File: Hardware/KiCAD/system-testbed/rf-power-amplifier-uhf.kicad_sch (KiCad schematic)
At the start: 22 parts, among them U5 GRF5604

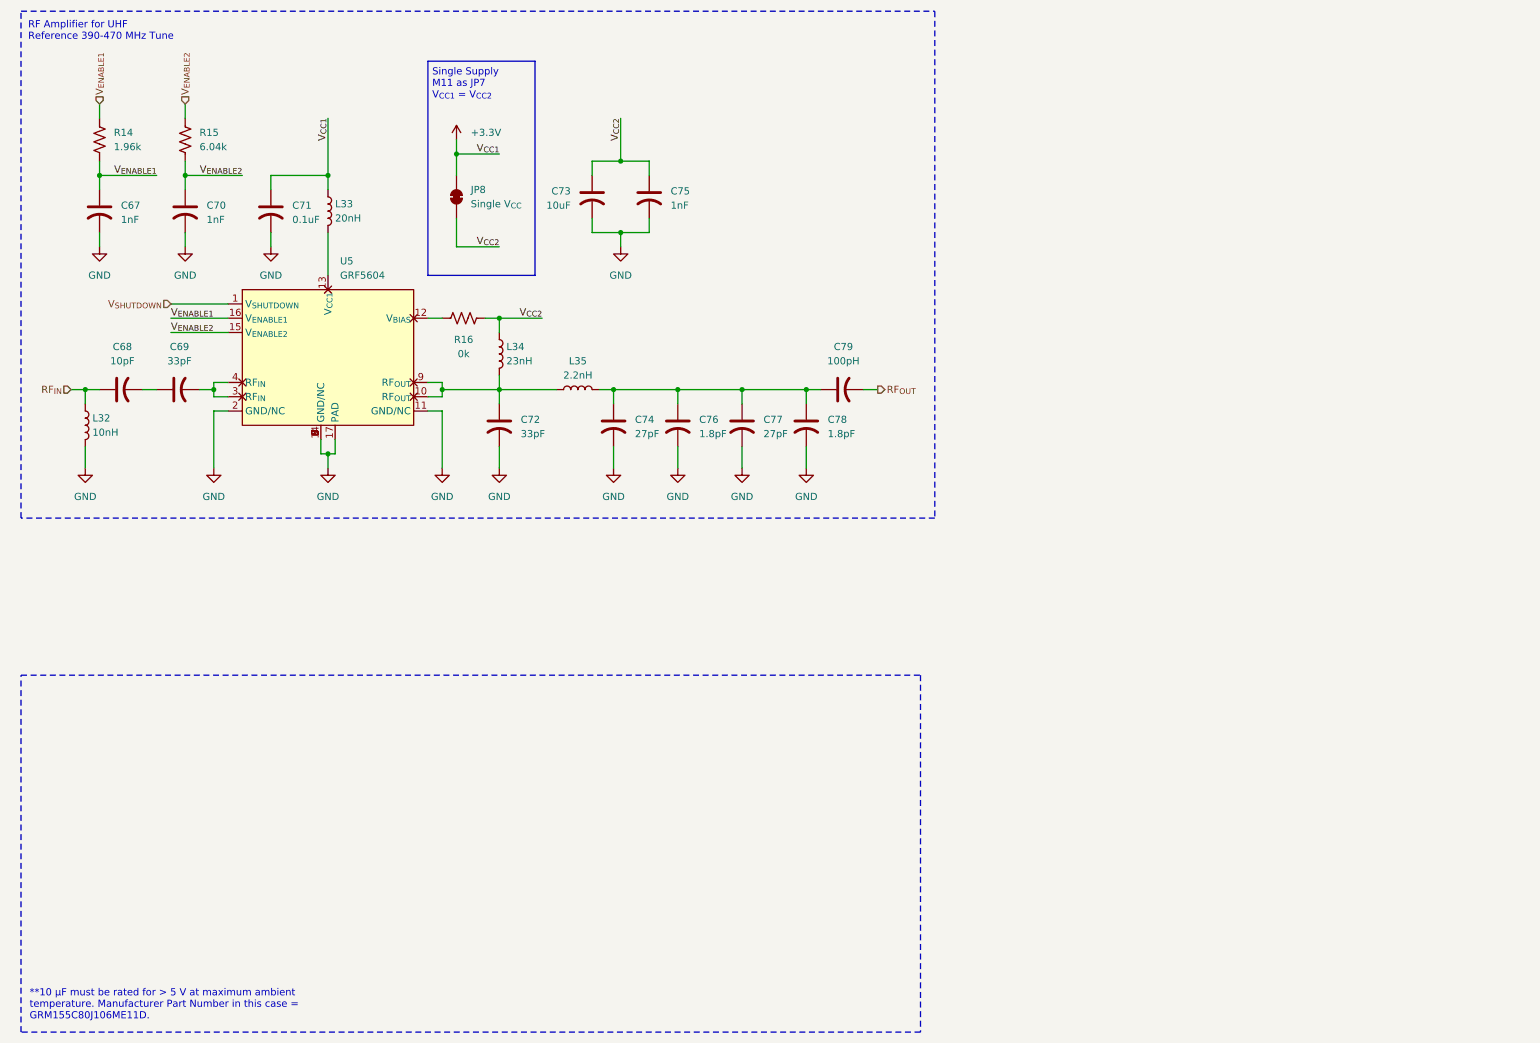
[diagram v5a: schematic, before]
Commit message: feat: separate RF subsystems for testing using SMA edge launches in testbed KiCAD project #65 #34 #45
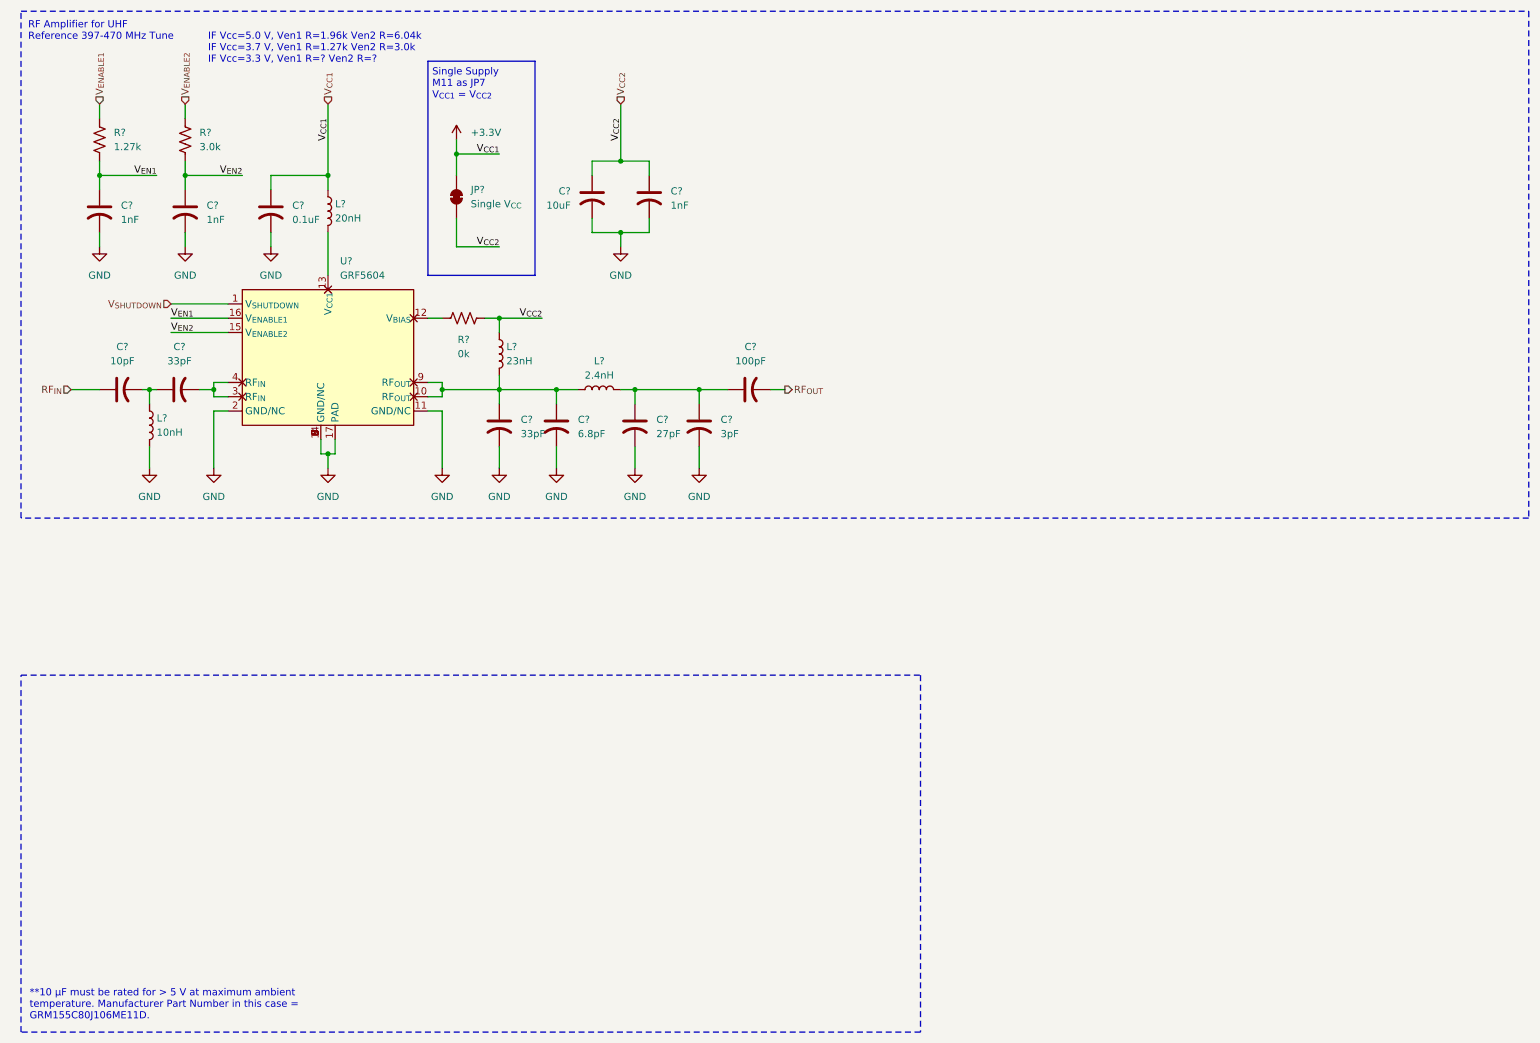
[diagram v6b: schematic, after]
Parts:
- removed C77: 27pF, Capacitor_SMD:C_0402_1005Metric, symbol Device:C_US
- removed C78: 1.8pF, Capacitor_SMD:C_0402_1005Metric, symbol Device:C_US
- added C?: 6.8pF, Capacitor_SMD:C_0402_1005Metric, symbol Device:C_US
- C?: renamed from C79; value 100pH -> 100pF
- C?: renamed from C76; value 1.8pF -> 3pF
- L?: renamed from L35; value 2.2nH -> 2.4nH
- L?: renamed from L34; footprint Inductor_SMD:L_0402_1005Metric -> capstone-project:0908SQ23NGLC
- R?: renamed from R14; value 1.96k -> 1.27k
- R?: renamed from R15; value 6.04k -> 3.0k
- renumbered C74 to C?, C69 to C?, C71 to C?, C75 to C?, C73 to C?, C67 to C?, C72 to C?, C70 to C?, C68 to C?, JP8 to JP?, L32 to L?, L33 to L?, R16 to R?, U5 to U?
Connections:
- net GND: now also C?.2
- net RF_{IN}: no longer L?.1
- net V_{ENABLE1}: no longer C?.1, R?.1, U?.16 (V_{ENABLE1})
- net V_{ENABLE2}: no longer C?.1, R?.1, U?.15 (V_{ENABLE2})
- net at C?.1, L?.1, L?.2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: now also C?.1
- net at C?.1, C?.2: now also L?.1
- new net V_{EN1}: C?.1, R?.1, U?.16 (V_{ENABLE1})
- new net V_{EN2}: C?.1, R?.1, U?.15 (V_{ENABLE2})
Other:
- note added: "IF Vcc=5.0 V, Ven1 R=1.96k Ven2 R=6.04k IF Vcc=3.7 V, Ven1 R=1.27k Ven2 R=3.0k IF Vcc=3.3 V, Ven1 R=? Ven2 R=?"
- note added: "RF Amplifier for UHF Reference 397-470 MHz Tune"
- note removed: "RF Amplifier for UHF Reference 390-470 MHz Tune"
- moved on the sheet: C?, L?
